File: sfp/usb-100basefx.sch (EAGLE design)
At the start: 53 parts, among them IC1 LD33, IC2 93LC66SN, Q1 MOSFET-NCHANNELBSS123LT1G, U1 AX88772BSP, U2 SFP, Y1 25MHz

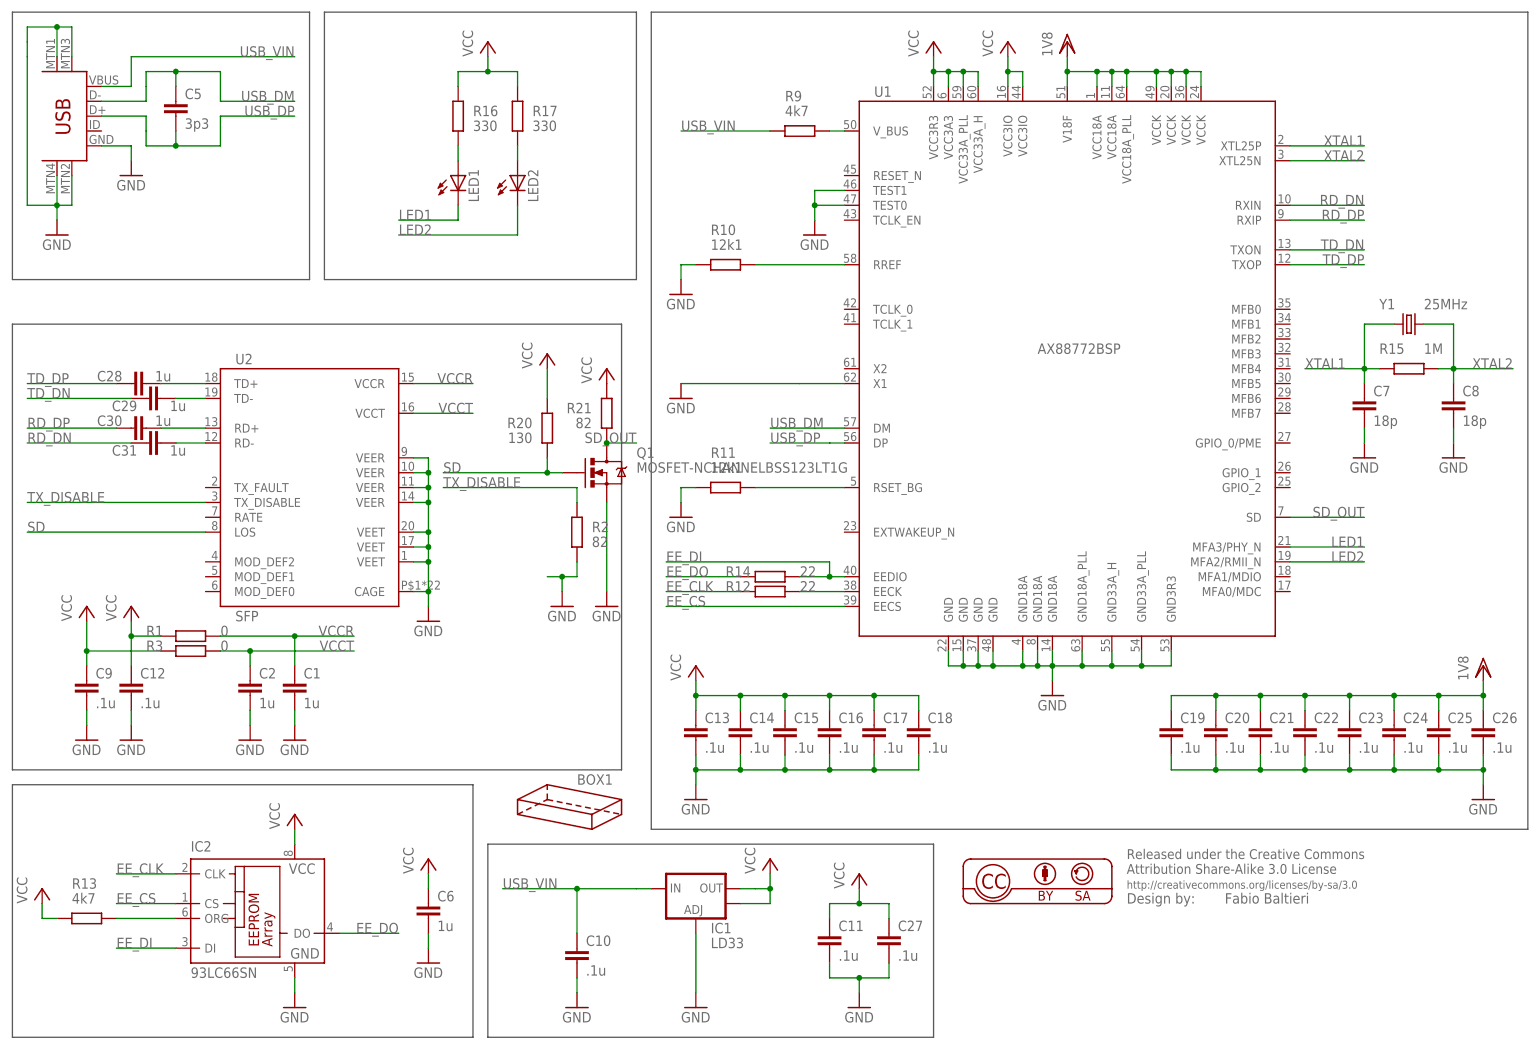
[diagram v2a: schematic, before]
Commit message: sfp: schematic cleanup
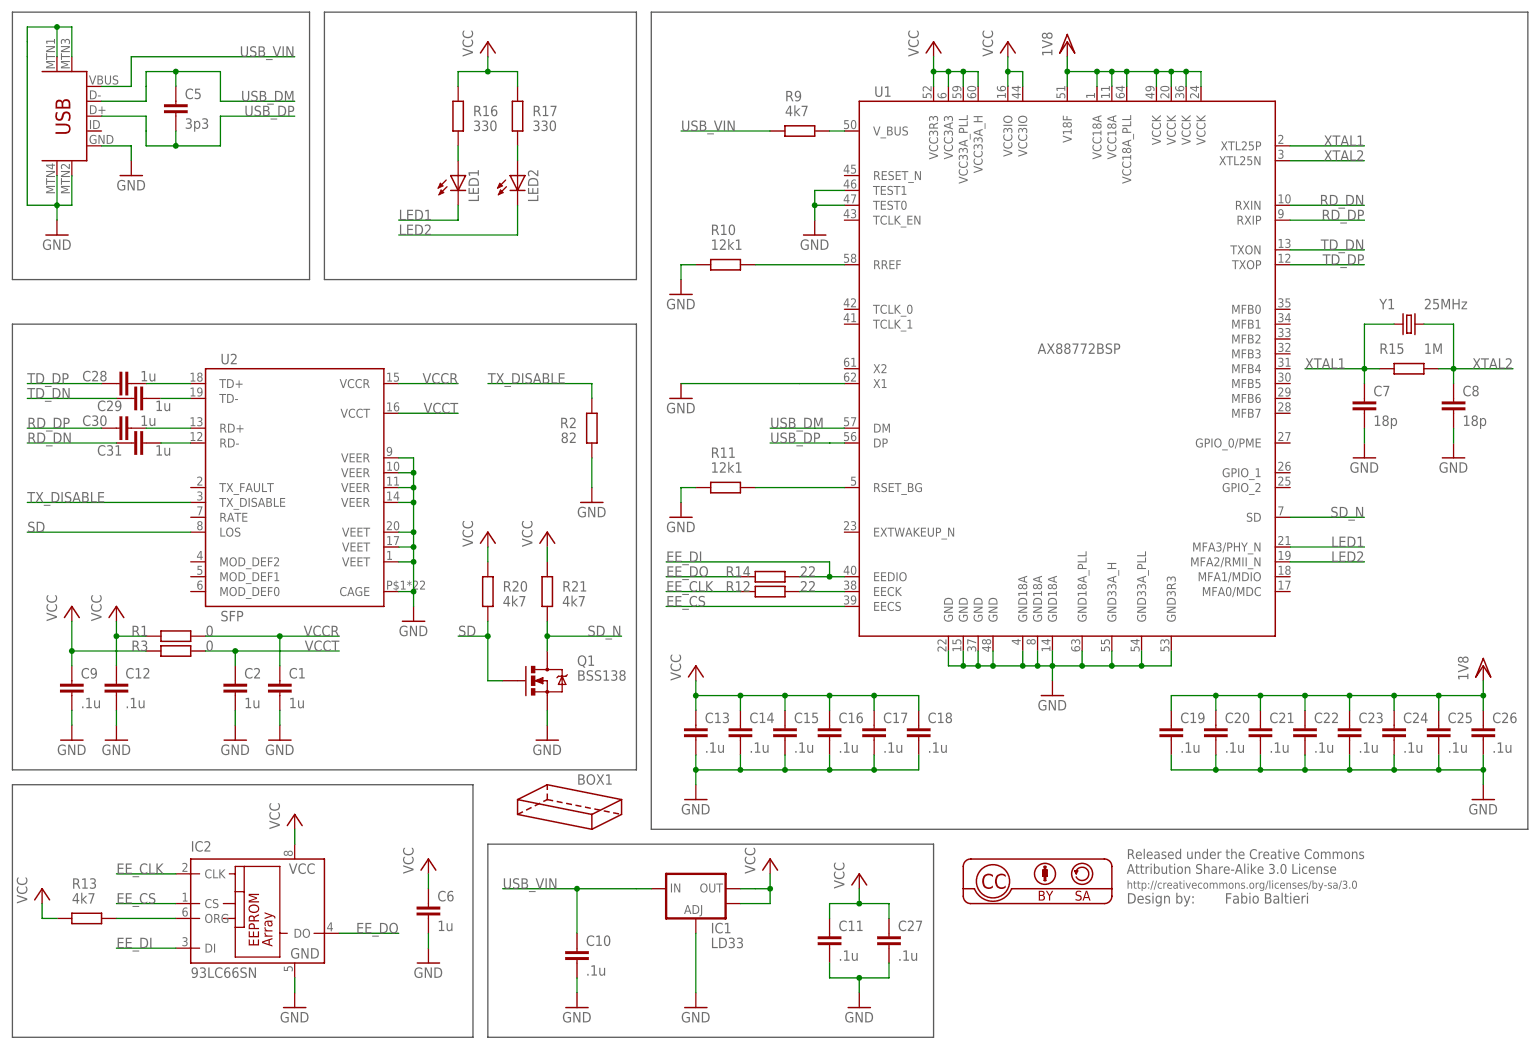
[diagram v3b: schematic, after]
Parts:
- Q1: value MOSFET-NCHANNELBSS123LT1G -> BSS138
- R20: value 130 -> 4k7
- R21: value 82 -> 4k7
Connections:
- net SD_OUT renamed SD_N
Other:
- moved on the sheet: C1, C12, C2, C28, C29, C30, C31, C9, Q1, R1, R2, R20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

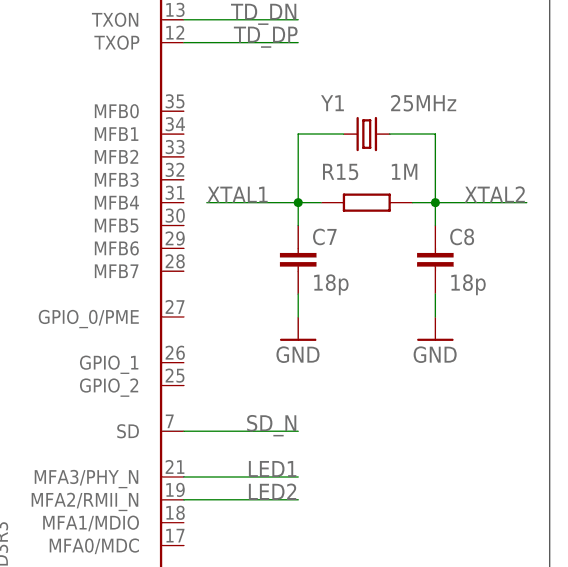
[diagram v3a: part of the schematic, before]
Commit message: sfp: change cap to 33p
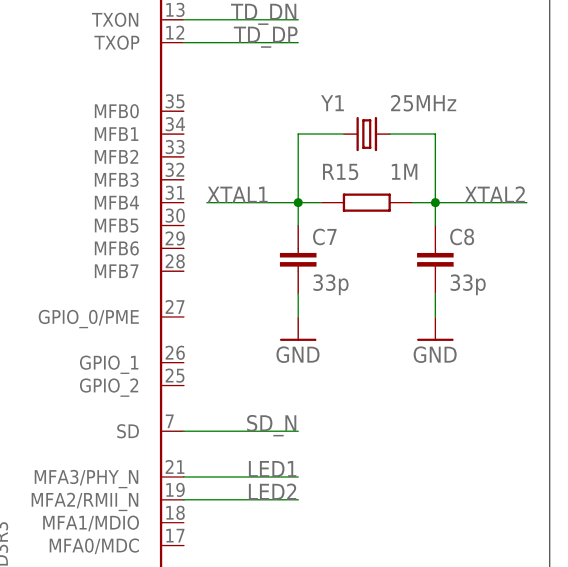
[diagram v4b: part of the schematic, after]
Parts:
- C7, C8: value 18p -> 33p
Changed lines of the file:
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@@
 <part name="GND12" library="supply1" deviceset="GND" device=""/>
 <part name="Y1" library="SparkFun-FreqCtrl" deviceset="CRYSTAL" device="5X3" value="25MHz"/>
-<part name="C7" library="rcl" deviceset="C-EU" device="C0603" value="18p"/>
-<part name="C8" library="rcl" deviceset="C-EU" device="C0603" value="18p"/>
+<part name="C7" library="rcl" deviceset="C-EU" device="C0603" value="33p"/>
+<part name="C8" library="rcl" deviceset="C-EU" device="C0603" value="33p"/>
 <part name="GND13" library="supply1" deviceset="GND" device=""/>
 <part name="GND14" library="supply1" deviceset="GND" device=""/>

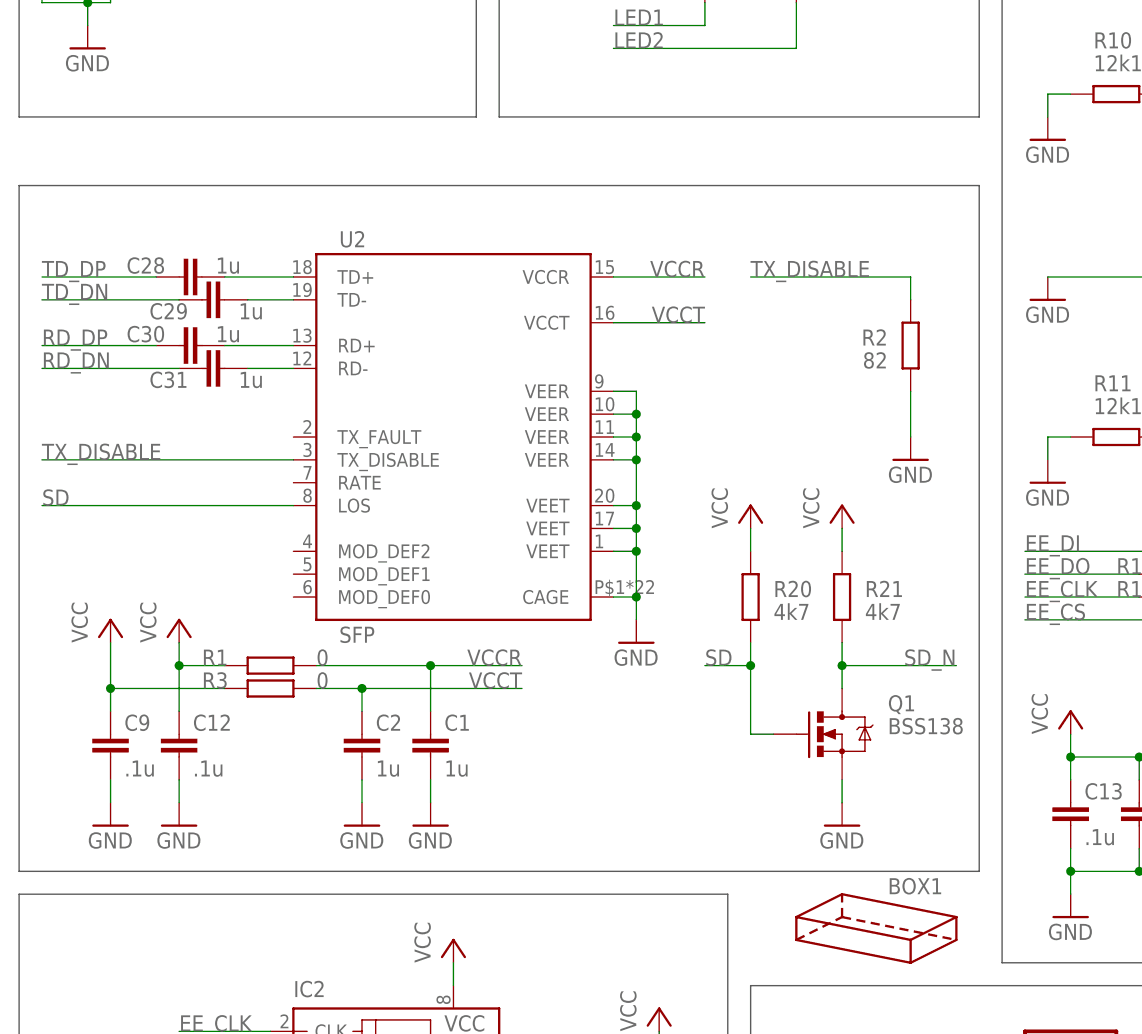
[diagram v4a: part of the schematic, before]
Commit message: sfp: add bias note
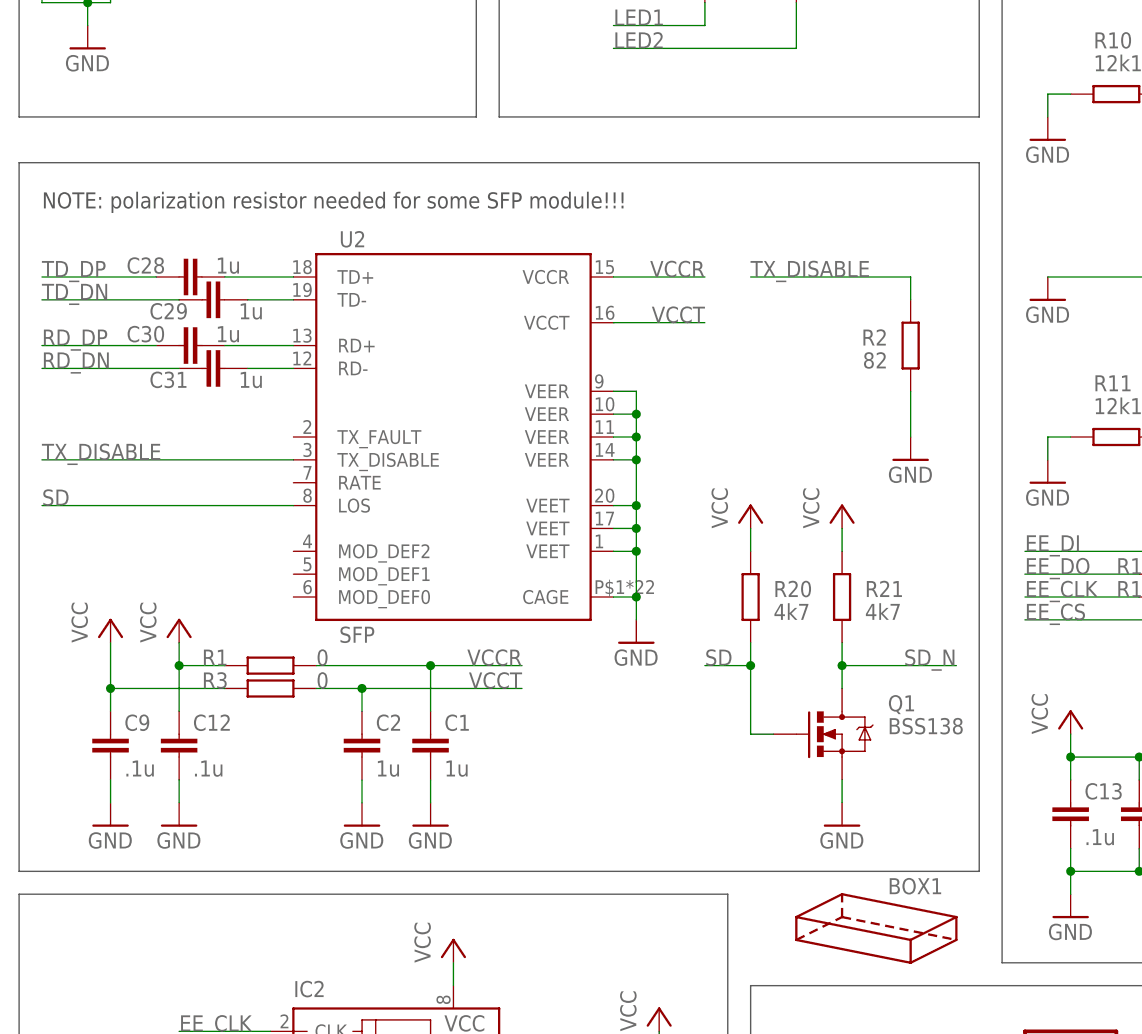
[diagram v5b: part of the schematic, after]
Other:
- note added: "NOTE: polarization resistor needed for some SFP module!!!"
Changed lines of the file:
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@@
 <wire x1="160.02" y1="2.54" x2="83.82" y2="2.54" width="0.1524" layer="97"/>
 <wire x1="83.82" y1="2.54" x2="83.82" y2="35.56" width="0.1524" layer="97"/>
-<wire x1="2.54" y1="124.46" x2="109.22" y2="124.46" width="0.1524" layer="97"/>
-<wire x1="109.22" y1="124.46" x2="109.22" y2="48.26" width="0.1524" layer="97"/>
+<wire x1="2.54" y1="127" x2="109.22" y2="127" width="0.1524" layer="97"/>
+<wire x1="109.22" y1="127" x2="109.22" y2="48.26" width="0.1524" layer="97"/>
 <wire x1="109.22" y1="48.26" x2="2.54" y2="48.26" width="0.1524" layer="97"/>
-<wire x1="2.54" y1="48.26" x2="2.54" y2="124.46" width="0.1524" layer="97"/>
+<wire x1="2.54" y1="48.26" x2="2.54" y2="127" width="0.1524" layer="97"/>
 <wire x1="111.76" y1="177.8" x2="261.62" y2="177.8" width="0.1524" layer="97"/>
 <wire x1="261.62" y1="177.8" x2="261.62" y2="38.1" width="0.1524" layer="97"/>
@@
 <wire x1="81.28" y1="45.72" x2="81.28" y2="2.54" width="0.1524" layer="97"/>
 <wire x1="81.28" y1="2.54" x2="2.54" y2="2.54" width="0.1524" layer="97"/>
+<text x="5.08" y="121.92" size="1.778" layer="97">NOTE: polarization resistor needed for some SFP module!!!</text>
 </plain>
 <instances>

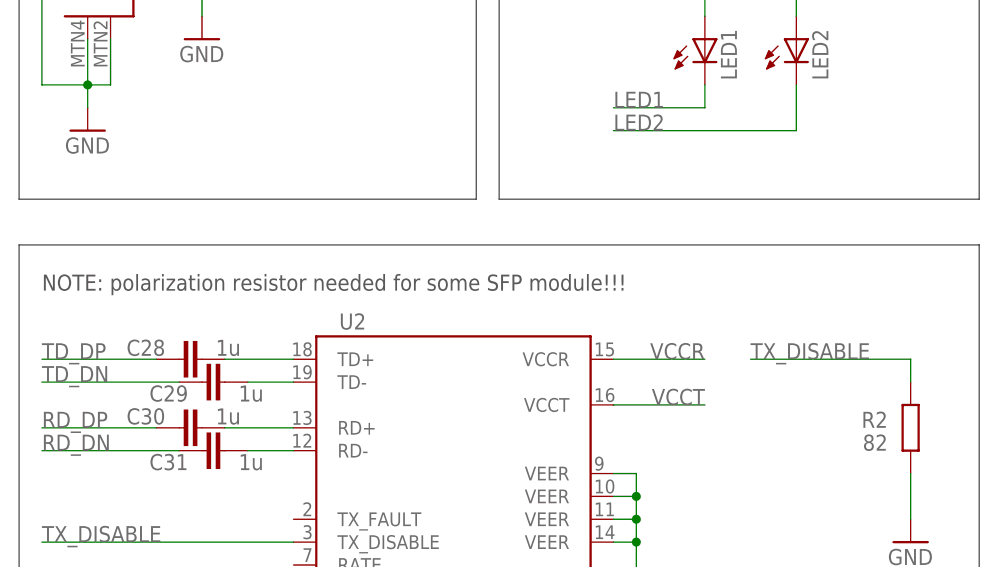
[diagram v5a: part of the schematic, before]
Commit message: sfp: reword biasing note
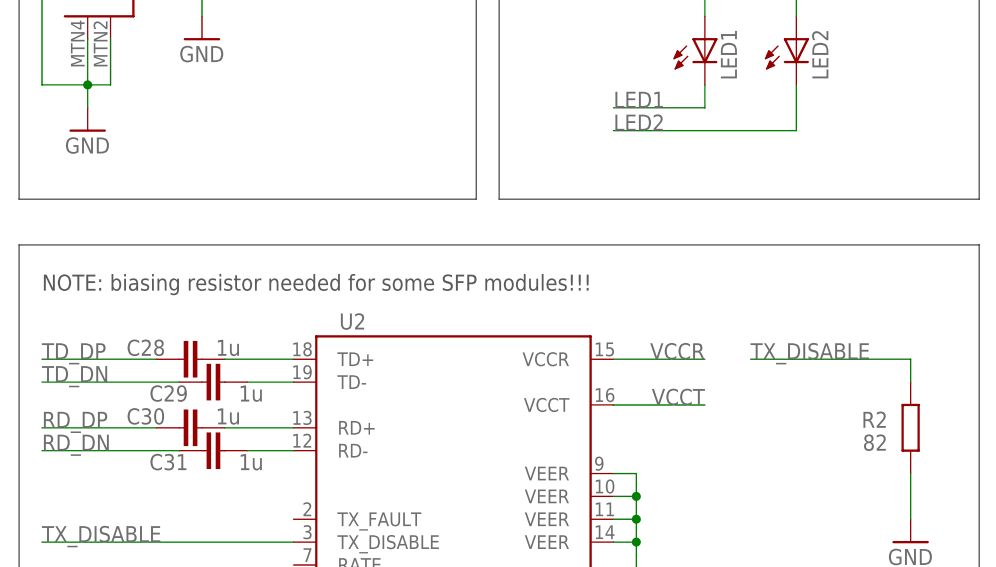
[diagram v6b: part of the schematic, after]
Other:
- note added: "NOTE: biasing resistor needed for some SFP modules!!!"
- note removed: "NOTE: polarization resistor needed for some SFP module!!!"
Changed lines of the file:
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@@
 <wire x1="81.28" y1="45.72" x2="81.28" y2="2.54" width="0.1524" layer="97"/>
 <wire x1="81.28" y1="2.54" x2="2.54" y2="2.54" width="0.1524" layer="97"/>
-<text x="5.08" y="121.92" size="1.778" layer="97">NOTE: polarization resistor needed for some SFP module!!!</text>
+<text x="5.08" y="121.92" size="1.778" layer="97">NOTE: biasing resistor needed for some SFP modules!!!</text>
 </plain>
 <instances>
